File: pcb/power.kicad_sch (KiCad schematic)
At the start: 22 parts, among them J3 Conn_01x02, J4 UJC-H-G-SMT-2-P6-TR, Q1 NTR4003N, SW3 SW_Push, U3 MCP73811T-420I-OT, U4 TLV77133PDBVR

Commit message: Simplify to minimum buck converter components
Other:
- title: (none) -> LMP91000 Portable Potentiostat
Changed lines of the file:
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@@
 	(generator_version "9.0")
 	(paper "A4")
+	(title_block
+		(title "LMP91000 Portable Potentiostat")
+	)
 	(rectangle
 		(start 12.7 63.5)

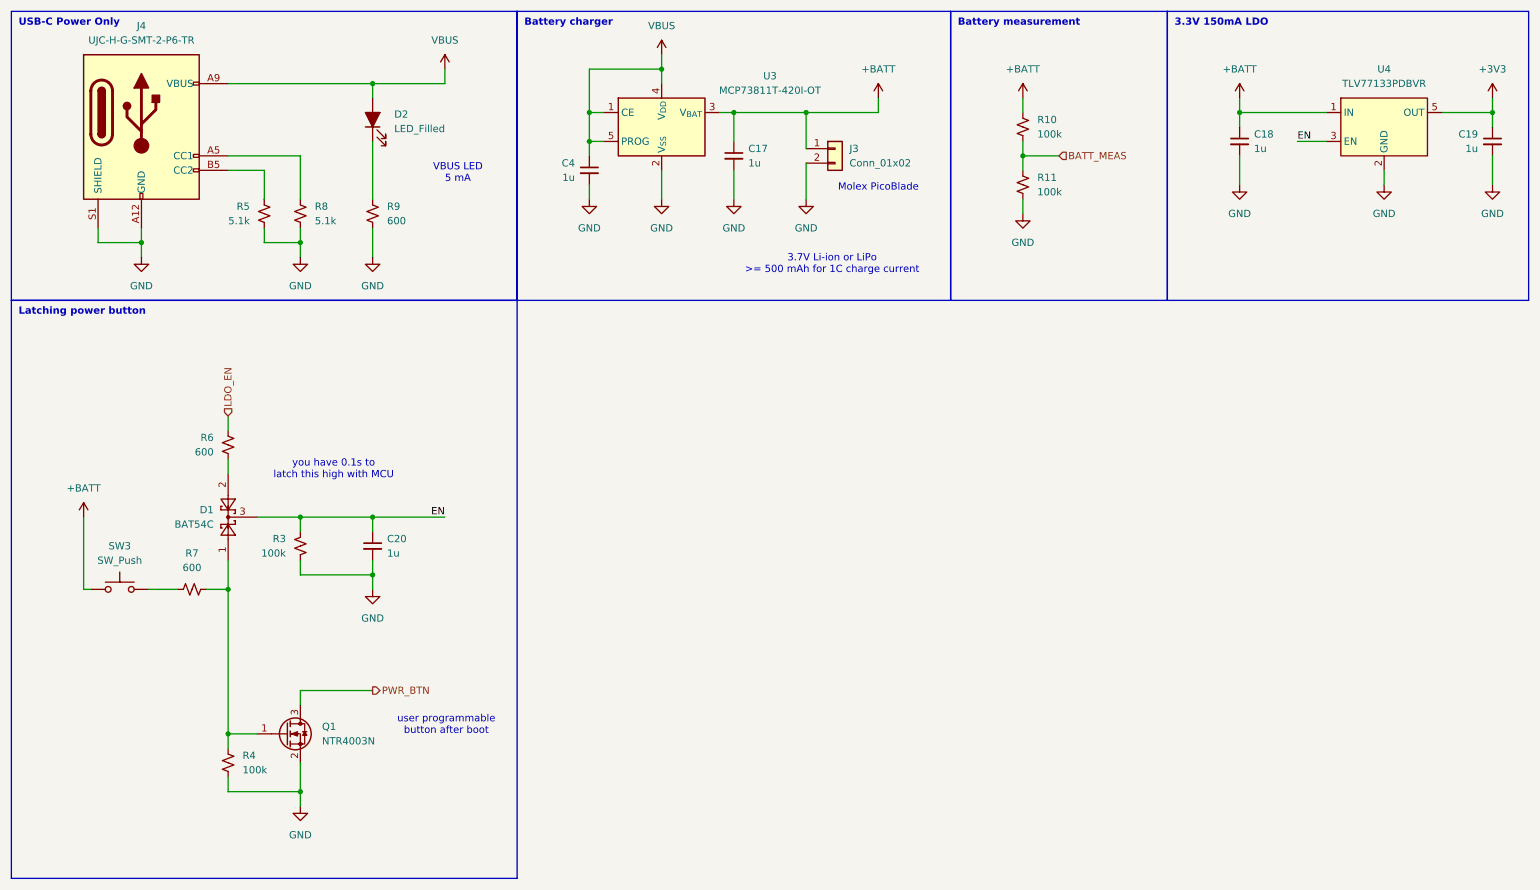
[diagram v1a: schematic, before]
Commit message: Assign footprints, cleanup schematics, start layout
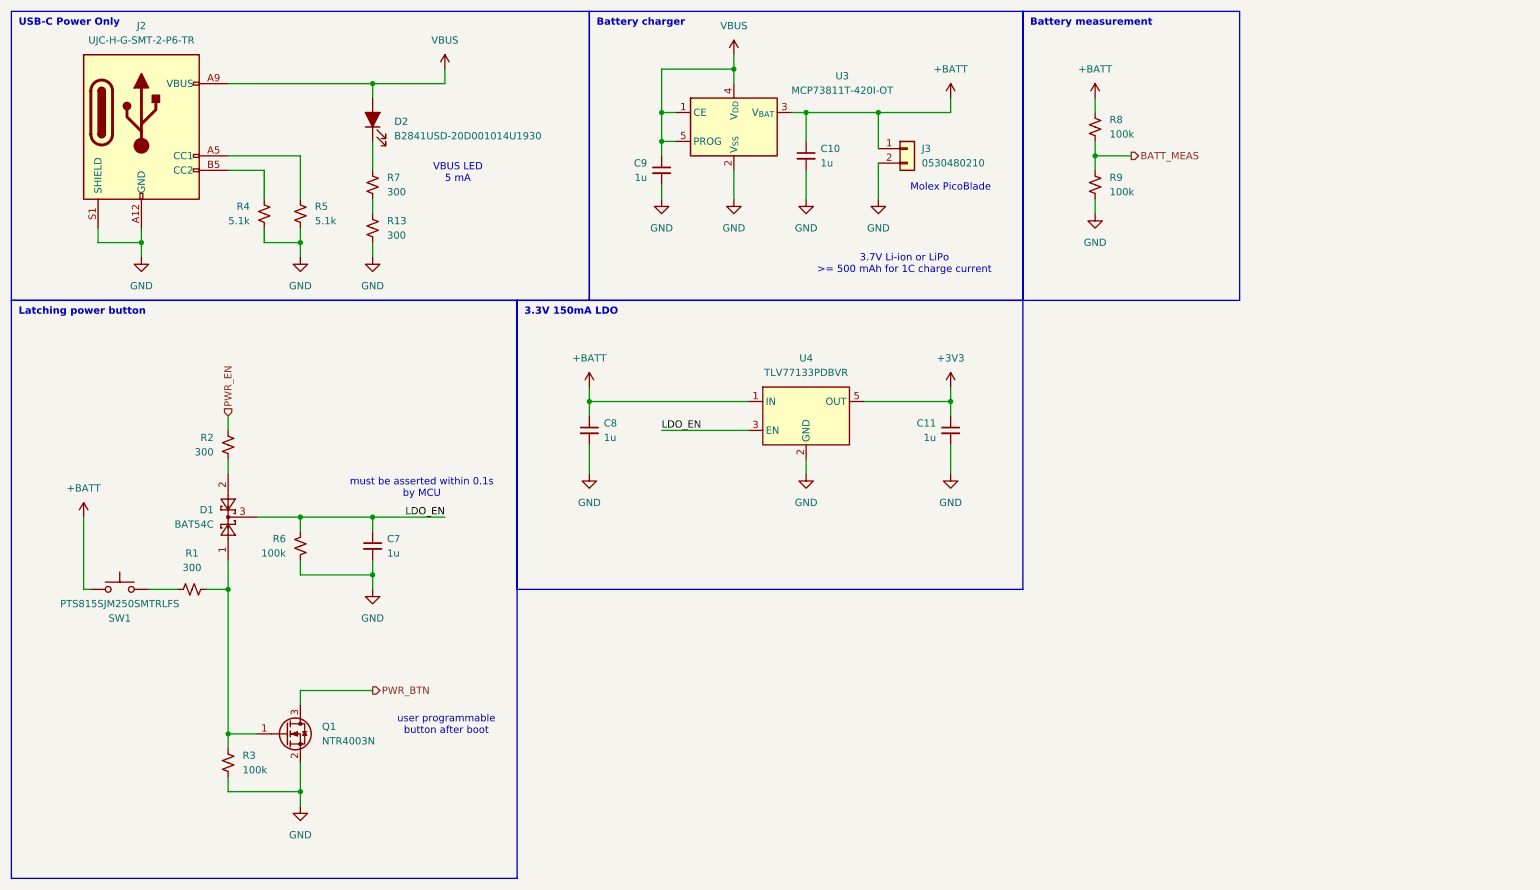
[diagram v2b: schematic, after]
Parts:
- added R13: 300, Resistor_SMD:R_0402_1005Metric, symbol Device:R_Small_US
- C10: renamed from C17; footprint (none) -> Capacitor_SMD:C_0402_1005Metric
- C11: renamed from C19; footprint (none) -> Capacitor_SMD:C_0402_1005Metric
- C7: renamed from C20; footprint (none) -> Capacitor_SMD:C_0402_1005Metric
- C8: renamed from C18; footprint (none) -> Capacitor_SMD:C_0402_1005Metric
- C9: renamed from C4; footprint (none) -> Capacitor_SMD:C_0402_1005Metric
- D2: value LED_Filled -> B2841USD-20D001014U1930; footprint (none) -> LED_SMD:LED_0402_1005Metric
- J2: renamed from J4; footprint (none) -> Connector_USB_SameSky:SAMESKY_UJC-H-G-SMT-2-P6-TR
- J3: value Conn_01x02 -> 0530480210; footprint (none) -> Connector_Molex:Molex_PicoBlade_53048-0210_1x02_P1.25mm_Horizontal
- R1: renamed from R7; value 600 -> 300; footprint (none) -> Resistor_SMD:R_0402_1005Metric
- R2: renamed from R6; value 600 -> 300; footprint (none) -> Resistor_SMD:R_0402_1005Metric
- R3: renamed from R4; footprint (none) -> Resistor_SMD:R_0402_1005Metric
- R4: renamed from R5; footprint (none) -> Resistor_SMD:R_0402_1005Metric
- R5: renamed from R8; footprint (none) -> Resistor_SMD:R_0402_1005Metric
- R6: renamed from R3; footprint (none) -> Resistor_SMD:R_0402_1005Metric
- R7: renamed from R9; value 600 -> 300; footprint (none) -> Resistor_SMD:R_0402_1005Metric
- R8: renamed from R10; footprint (none) -> Resistor_SMD:R_0402_1005Metric
- R9: renamed from R11; footprint (none) -> Resistor_SMD:R_0402_1005Metric
- SW1: renamed from SW3; value SW_Push -> PTS815SJM250SMTRLFS; footprint (none) -> PTS815_SJM_250_SMTR_LFS:SW_Push_PTS815_SJM_250_SMTR_LFS
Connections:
- net EN is gone; now on net LDO_EN: C7.1, D1.3, R6.1, U4.3 (EN)
- net GND: now also R13.2; no longer R7.2
- net LDO_EN: no longer R2.1
- new net: R13.1, R7.2
- new net PWR_EN: R2.1
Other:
- note added: "must be asserted within 0.1s by MCU"
- note removed: "you have 0.1s to latch this high with MCU"
- company: (none) -> Clarkson University
- moved on the sheet: C10, C11, C8, C9, J3, R7, R8, R9, U3, U4

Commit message: Move antenna and tag connect
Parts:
- C10, C11, C7, C8, C9: HQ_MPN (none) -> CL05X105KP5NNNC
- D1: HQ_MPN (none) -> DS0140568
- D2: HQ_MPN (none) -> F.0402.00003/P2-0402R1TS2-045T-001
- J2: HQ_MPN (none) -> UJC-H-G-SMT-2-P6-TR
- J3: HQ_MPN (none) -> 530480210
- Q1: HQ_MPN (none) -> DS0188329
- R1, R13, R2, R7: HQ_MPN (none) -> RTT02301JTH
- R3, R6, R8, R9: HQ_MPN (none) -> WR04X1003FTL
- R4, R5: HQ_MPN (none) -> WR04X5101FTL
- SW1: HQ_MPN (none) -> SKRPADE010
- U3: HQ_MPN (none) -> MCP73811T-420I/OT
- U4: HQ_MPN (none) -> TLV77133PDBVR
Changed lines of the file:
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@@
+			)
+		)
+		(property "HQ_MPN" "RTT02301JTH"
+			(at 44.45 114.3 90)
+			(effects
+				(font
+					(size 1.27 1.27)
+				)
+				(hide yes)
 			)
 		)
@@
 			)
 		)
+		(property "HQ_MPN" "DS0140568"
+			(at 50.8 101.6 90)
+			(effects
+				(font
+					(size 1.27 1.27)
+				)
+				(hide yes)
+			)
+		)
 		(pin "3"
 		)
@@
 			)
 		)
+		(property "HQ_MPN" "CL05X105KP5NNNC"
+			(at 76.2 106.68 0)
+			(effects
+				(font
+					(size 1.27 1.27)
+				)
+				(hide yes)
+			)
+		)
 		(pin "2"
 		)
@@
 			)
 		)
+		(property "HQ_MPN" "CL05X105KP5NNNC"
+			(at 152.4 38.1 0)
+			(effects
+				(font
+					(size 1.27 1.27)
+				)
+				(hide yes)
+			)
+		)
 		(pin "1"
 		)
@@
 		)
 		(property "Description" "Resistor, small US symbol"
+			(at 76.2 50.8 0)
+			(effects
+				(font
+					(size 1.27 1.27)
+				)
+				(hide yes)
+			)
+		)
+		(property "HQ_MPN" "RTT02301JTH"
 			(at 76.2 50.8 0)
 			(effects
@@
 			)
 		)
+		(property "HQ_MPN" "CL05X105KP5NNNC"
+			(at 127 40.64 0)
+			(effects
+				(font
+					(size 1.27 1.27)
+				)
+				(hide yes)
+			)
+		)
 		(pin "1"
 		)
@@
 			)
 		)
+		(property "HQ_MPN" "F.0402.00003/P2-0402R1TS2-045T-001 "
+			(at 76.2 31.75 90)
+			(effects
+				(font
+					(size 1.27 1.27)
+				)
+				(hide yes)
+			)
+		)
 		(pin "1"
 		)
@@
 			)
 		)
+		(property "HQ_MPN" "UJC-H-G-SMT-2-P6-TR"
+			(at 35.56 33.02 0)
+			(effects
+				(font
+					(size 1.27 1.27)
+				)
+				(hide yes)
+			)
+		)
 		(pin "A5"
 		)
@@
 			)
 		)
+		(property "HQ_MPN" "DS0188329"
+			(at 60.96 139.7 0)
+			(effects
+				(font
+					(size 1.27 1.27)
+				)
+				(hide yes)
+			)
+		)
 		(pin "3"
 		)
@@
 			)
 		)
+		(property "HQ_MPN" "WR04X1003FTL"
+			(at 203.2 33.02 0)
+			(effects
+				(font
+					(size 1.27 1.27)
+				)
+				(hide yes)
+			)
+		)
 		(pin "2"
 		)
@@
 			)
 		)
+		(property "HQ_MPN" "RTT02301JTH"
+			(at 50.8 88.9 0)
+			(effects
+				(font
+					(size 1.27 1.27)
+				)
+				(hide yes)
+			)
+		)
 		(pin "2"
 		)
@@
 			)
 		)
+		(property "HQ_MPN" "WR04X1003FTL"
+			(at 203.2 43.18 0)
+			(effects
+				(font
+					(size 1.27 1.27)
+				)
+				(hide yes)
+			)
+		)
 		(pin "2"
 		)
@@
 			)
 		)
+		(property "HQ_MPN" "MCP73811T-420I/OT"
+			(at 139.7 33.02 0)
+			(effects
+				(font
+					(size 1.27 1.27)
+				)
+				(hide yes)
+			)
+		)
 		(pin "4"
 		)
@@
 			)
 		)
+		(property "HQ_MPN" "CL05X105KP5NNNC"
+			(at 114.3 86.36 0)
+			(effects
+				(font
+					(size 1.27 1.27)
+				)
+				(hide yes)
+			)
+		)
 		(pin "1"
 		)
@@
 		)
 		(property "Description" "Generic connector, single row, 01x02, script generated (kicad-library-utils/schlib/autogen/connector/)"
+			(at 170.18 36.83 0)
+			(effects
+				(font
+					(size 1.27 1.27)
+				)
+				(hide yes)
+			)
+		)
+		(property "HQ_MPN" "530480210"
 			(at 170.18 36.83 0)
 			(effects
@@
 			)
 		)
+		(property "HQ_MPN" "CL05X105KP5NNNC"
+			(at 177.8 86.36 0)
+			(effects
+				(font
+					(size 1.27 1.27)
+				)
+				(hide yes)
+			)
+		)
 		(pin "1"
 		)
@@
 			)
 		)
+		(property "HQ_MPN" "WR04X5101FTL"
+			(at 57.15 48.26 0)
+			(effects
+				(font
+					(size 1.27 1.27)
+				)
+				(hide yes)
+			)
+		)
 		(pin "2"
 		)
@@
 			)
 		)
+		(property "HQ_MPN" "RTT02301JTH"
+			(at 76.2 43.18 0)
+			(effects
+				(font
+					(size 1.27 1.27)
+				)
+				(hide yes)
+			)
+		)
 		(pin "1"
 		)
@@
 			)
 		)
+		(property "HQ_MPN" "WR04X5101FTL"
+			(at 63.5 48.26 0)
+			(effects
+				(font
+					(size 1.27 1.27)
+				)
+				(hide yes)
+			)
+		)
 		(pin "2"
 		)
@@
 			)
 		)
+		(property "HQ_MPN" "WR04X1003FTL"
+			(at 50.8 144.78 0)
+			(effects
+				(font
+					(size 1.27 1.27)
+				)
+				(hide yes)
+			)
+		)
 		(pin "2"
 		)
@@
 		)
 		(property "Description" "Push button switch, generic, two pins"
+			(at 31.75 114.3 0)
+			(effects
+				(font
+					(size 1.27 1.27)
+				)
+				(hide yes)
+			)
+		)
+		(property "HQ_MPN" "SKRPADE010"
 			(at 31.75 114.3 0)
 			(effects
@@
 			)
 		)
+		(property "HQ_MPN" "WR04X1003FTL"
+			(at 63.5 106.68 0)
+			(effects
+				(font
+					(size 1.27 1.27)
+				)
+				(hide yes)
+			)
+		)
 		(pin "2"
 		)
@@
 			(effects
 				(font
+					(size 1.27 1.27)
+				)
+				(hide yes)
+			)
+		)
+		(property "HQ_MPN" "TLV77133PDBVR"
+			(at 152.4 78.74 0)
+			(effects
+				(font

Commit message: Create Simplicity Studio 6 firmware project
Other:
- note added: "max 2.1V at full charge to 1.75V when discarged to LDO cutoff"
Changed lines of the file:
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@@
+		)
+	)
+	(text "max 2.1V at full charge\nto 1.75V when discarged to LDO cutoff"
+		(exclude_from_sim no)
+		(at 210.058 60.198 0)
+		(effects
+			(font
+				(size 1.27 1.27)
+			)
 		)
 	)
@@
 	(wire
 		(pts
-			(xy 76.2 132.08) (xy 63.5 132.08)
-		)
-		(stroke
+			(xy 63.5 132.08) (xy 76.2 132.08)
+		)
+		(stroke
